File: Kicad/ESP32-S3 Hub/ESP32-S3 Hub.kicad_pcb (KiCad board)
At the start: 6 copper layers, 15 x 30 mm, 57 parts, among them J1 1.27mm 3pin socket, J10 1.27mm 3pin socket, J11 7 pin FPC 0.3mm Panasonic Y3b, J12 1.27mm 3pin socket, J13 TE 3-2363961-0 receptacle, J14 TE 3-2363962-0 Connector, J16 TE 3-2363961-0 receptacle, J17 TE 3-2363962-0 Connector, J2 1.27mm 3pin socket, J21 1.27mm 4 pin socket, J22 1.27mm 4 pin header, J3 7 pin FPC 0.3mm Panasonic Y3b, J4 1.27mm 3pin socket, J5 7 pin FPC 0.3mm Panasonic Y3b, J6 1.27mm 3pin socket, J7 1.27mm 3pin socket, J8 7 pin FPC 0.3mm Panasonic Y3b, J9 1.27mm 3pin socket, SW1 Mitsumi R-667996, SW2 Mitsumi R-667996, U1 ESP32-S3, U2 74HC595, U3 THVD1420DRLR, Y1 ABM11-40.000MHZ-B1U-T3, 10ppm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

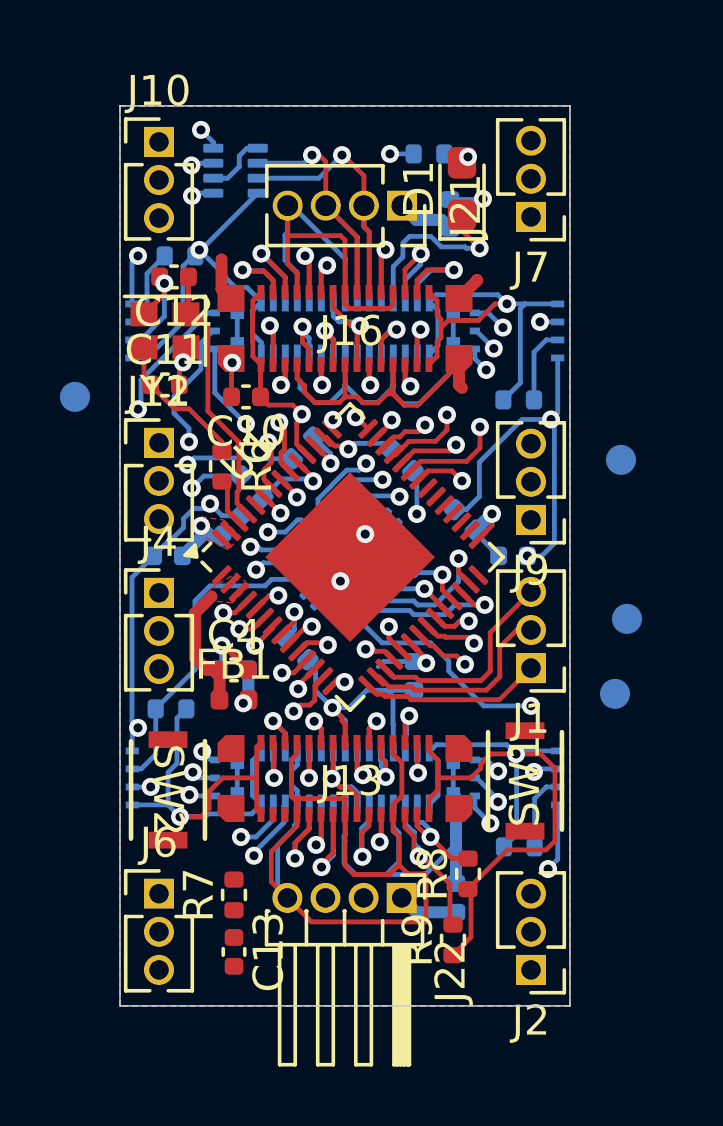
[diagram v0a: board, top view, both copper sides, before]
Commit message: Routed UART, buttons, and flipped analog power cap
I needed a capacitor near the power input at the top, because otherwise the power is flowing directly from the plane through the one via. I'm still not sure that I've fixed a problem, its seems likely that the main power flowing so close to the chips pins is a bad idea.
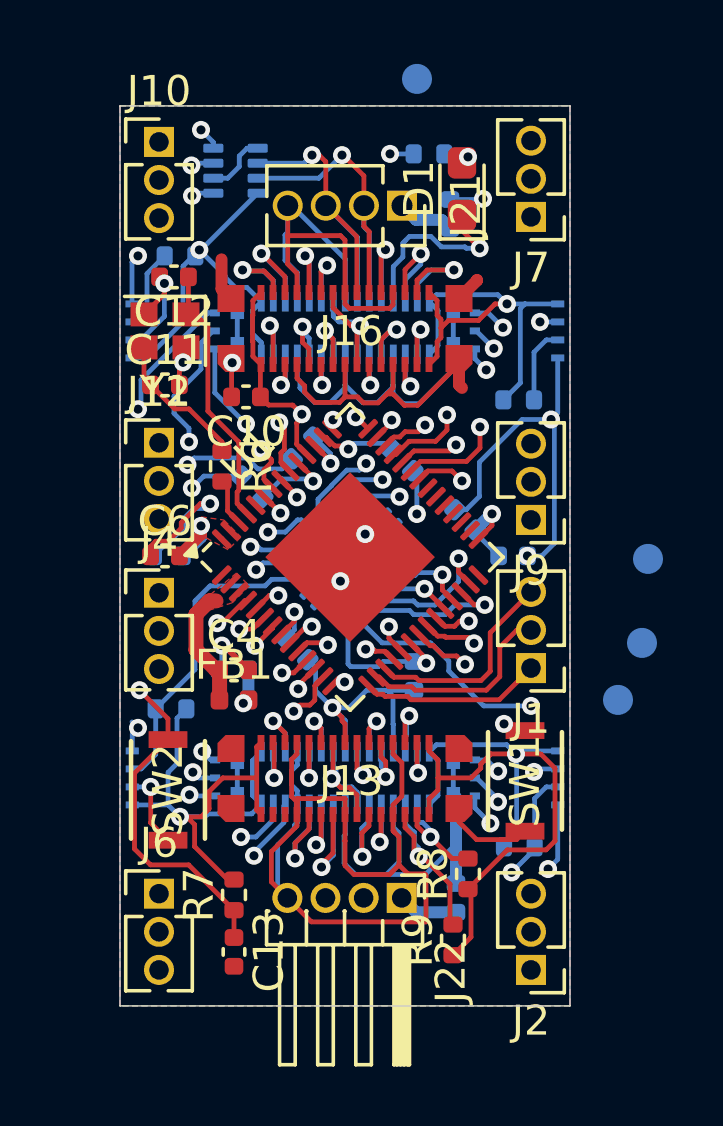
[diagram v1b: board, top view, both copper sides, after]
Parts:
- C6: moved to F.Cu
- moved TP20 15.6 mm to (157.8, 80.9)
- moved TP14 3.42 mm to (165.5, 96.9)
- moved C6 2.42 mm to (149.4, 96.8), turned to 0 degrees
- moved TP12 0.94 mm to (165.3, 99.7)
- moved TP1 0.22 mm to (164.5, 101.6)
- turned SW2 to 90 degrees
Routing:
- net UART0_TX: track 1.58 -> 19.6 mm
- net NRST: track 0.97 -> 16.6 mm, vias 1 -> 2
- net BOOT: track 0.94 -> 16.0 mm, vias 1 -> 2
- net UART0-RTS/CS0: track 2.62 -> 12.6 mm
- net UART0_RX: track 2.54 -> 12.3 mm
- net CS1: track 10.1 -> 17.6 mm, vias 1 -> 2
- net VDD: track 146.4 -> 152.1 mm
- net LED: track 22.6 -> 24.1 mm
- net GND: track 151.3 -> 152.7 mm
- net SDA1: track 47.3 -> 46.4 mm
- net CS5: track 22.6 -> 21.8 mm

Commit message: Routed Free 1 and 2 pins
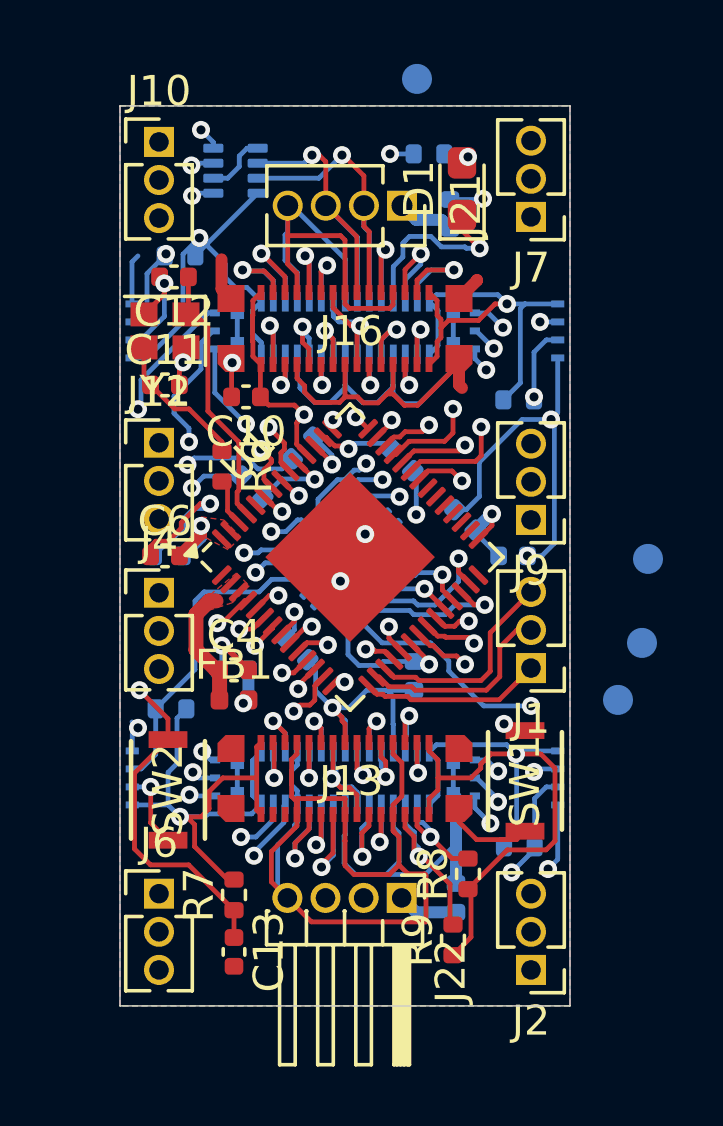
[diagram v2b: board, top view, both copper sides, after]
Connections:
- U1 pad 40: Free1 -> Free2
- U1 pad 41: Free2 -> Free1
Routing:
- net Free2: track 20.9 -> 36.7 mm
- net CS3: track 4.12 -> 16.6 mm, vias 1 -> 2
- net CS4: track 5.23 -> 17.1 mm, vias 1 -> 2
- net Free1: track 16.3 -> 23.0 mm
- net VDD: track 152.1 -> 157.4 mm
- net UART0_TX: track 19.6 -> 15.4 mm
- net SCL1: track 53.6 -> 51.7 mm
- net GND: vias 18 -> 17

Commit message: Swapped header logical numbers
I realized my numbering scheme was off with the actual board layout. So in the schematic I swapped the connectors without rewiring so that the numbers are more logical. CS7, CS8, and Free2 are now for the top mezzanine connector, which is closer to the pins on the chips. It also falls in line with my bottom up numbering scheme.
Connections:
- J13 pad 22: Free2 -> Free1
- J13 pad 26: CS8 -> CS6
- J13 pad 28: CS7 -> CS5
- J13 pad 3: CS7 -> CS5
- J13 pad 5: CS8 -> CS6
- J13 pad 9: Free2 -> Free1
- J14 pad 10: Free2 -> Free1
- J14 pad 21: Free2 -> Free1
- J14 pad 25: CS8 -> CS6
- J14 pad 27: CS7 -> CS5
- J14 pad 4: CS7 -> CS5
- J14 pad 6: CS8 -> CS6
- J16 pad 22: Free1 -> Free2
- J16 pad 26: CS6 -> CS8
- J16 pad 28: CS5 -> CS7
- J16 pad 3: CS5 -> CS7
- J16 pad 5: CS6 -> CS8
- J16 pad 9: Free1 -> Free2
- J17 pad 10: Free1 -> Free2
- J17 pad 21: Free1 -> Free2
- J17 pad 25: CS6 -> CS8
- J17 pad 27: CS5 -> CS7
- J17 pad 4: CS5 -> CS7
- J17 pad 6: CS6 -> CS8
- U1 pad 40: Free2 -> Free1
- U1 pad 41: Free1 -> Free2
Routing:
- net Free2: track 36.7 -> 23.0 mm
- net Free1: track 23.0 -> 36.7 mm
- net CS8: track 15.7 -> 28.0 mm
- net CS6: track 29.5 -> 17.2 mm
- net CS5: track 21.6 -> 12.4 mm
- net CS7: track 13.1 -> 22.3 mm

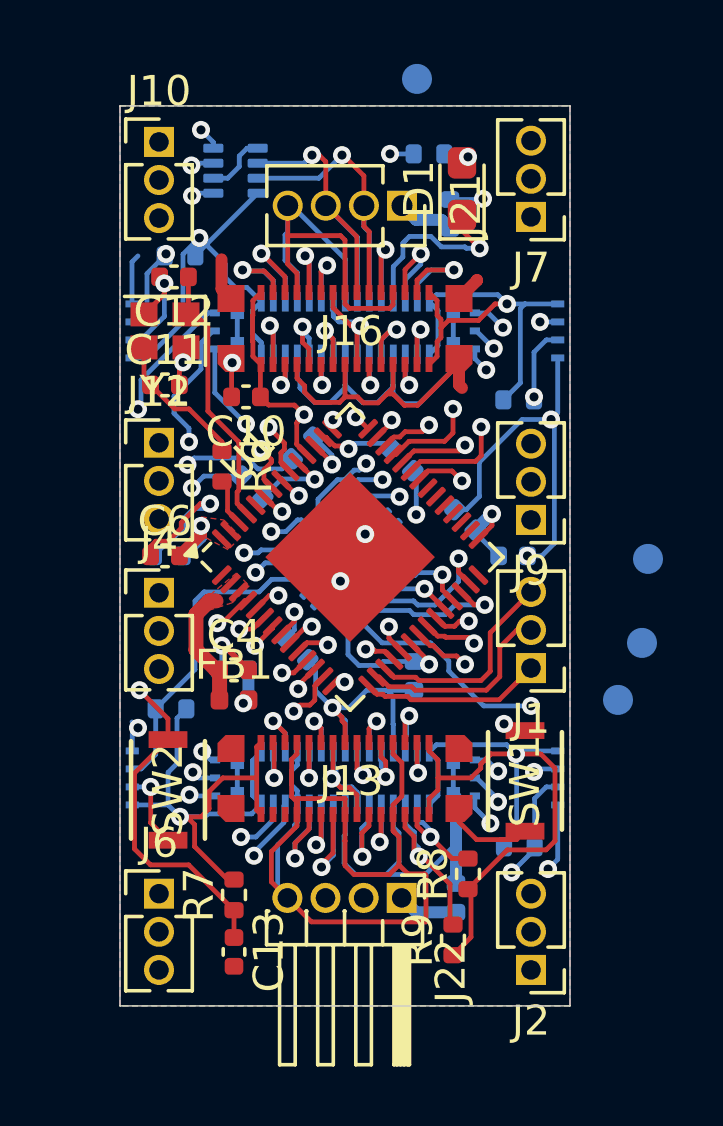
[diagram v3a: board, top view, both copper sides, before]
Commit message: Finished routing PWM motor pins
I did have to sacrifice the continuity of one of my ground planes to make it happen though. I tried to keep it to a minimum
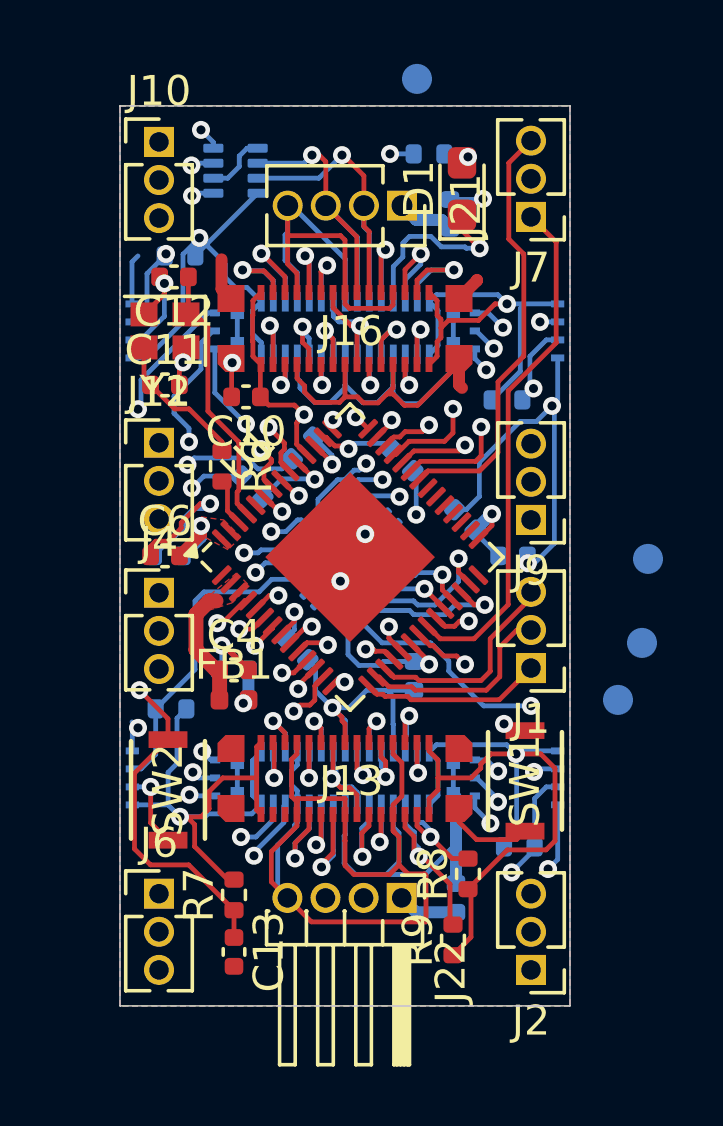
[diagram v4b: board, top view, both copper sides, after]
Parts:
- moved R19 0.39 mm to (160.8, 91.6)
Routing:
- net 4A: track 3.53 -> 21.6 mm
- net 3B: track 1.28 -> 17.6 mm
- net 4B: track 2.34 -> 18.6 mm
- net 3A: track 1.79 -> 17.3 mm, vias 1 -> 0
- net 4C: track 3.07 -> 16.4 mm
- net 3C: track 1.69 -> 14.3 mm, vias 1 -> 0
- net 2C: track 1.94 -> 14.5 mm
- net 2B: track 1.01 -> 11.4 mm
- net 2A: track 1.08 -> 10.3 mm
- net CS3: track 16.6 -> 17.1 mm
- added copper zone on In2.Cu, net VDD
- removed copper zone on In3.Cu, net VDD

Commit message: Finished basic routing
Now I have to fix some things to try and reduce crosstalk, and improve signal integrity. The likelihood of me being able to completely fix it is low, due to limited space. I also have to run the DRC, and fix the silkscreen.
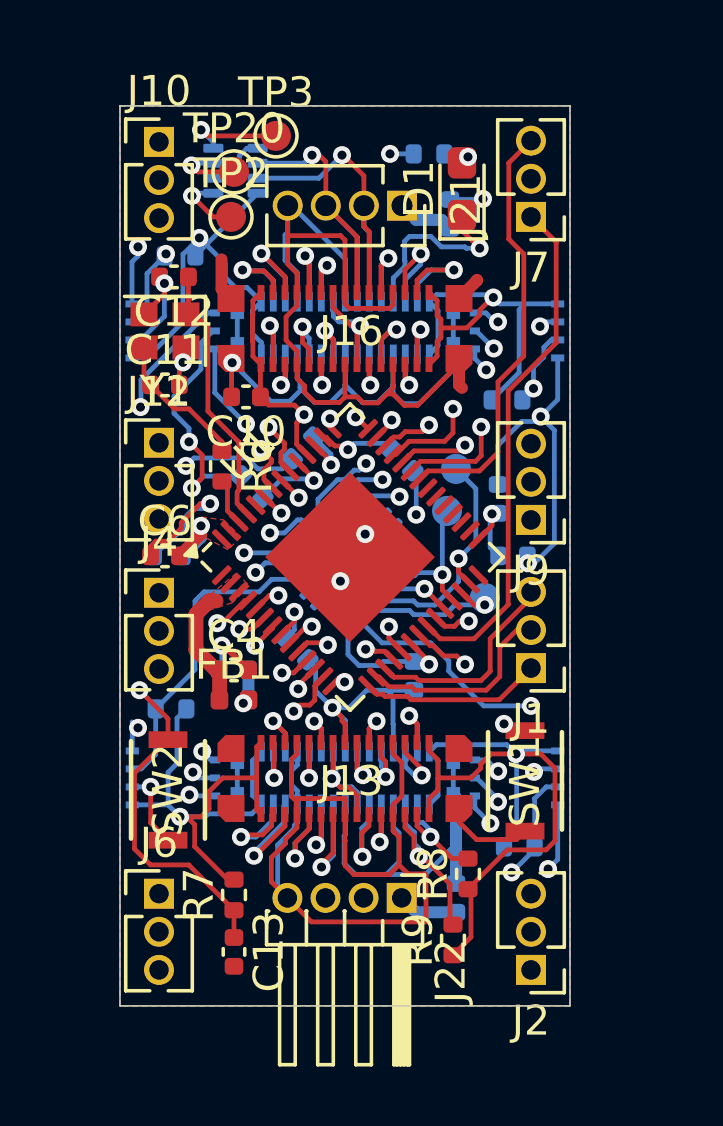
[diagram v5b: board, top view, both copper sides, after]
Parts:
- added TP2: ~, TestPoint:TestPoint_Pad_D1.0mm, F.Cu at (151.6, 85.5)
- added TP3: ~, TestPoint:TestPoint_Pad_D1.0mm, F.Cu at (153.1, 82.8)
- TP20: moved to F.Cu
- moved TP1 9.40 mm to (159.1, 93.9)
- moved TP12 7.85 mm to (158.8, 95.3)
- moved TP20 6.84 mm to (151.7, 84.0), turned to 0 degrees
- moved TP14 5.60 mm to (160.1, 98.2)
- moved C7 1.30 mm to (160.5, 94.9), turned to 90 degrees
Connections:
- TP1 pad 1: ShiftRegCLK -> ShiftEn
- U1 pad 6: 4CSA-B -> 4CSA-A
- U1 pad 7: 4CSA-A -> 4CSA-B
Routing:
- net MISO1: track 38.4 -> 105.8 mm
- net SCK1: track 18.2 -> 65.8 mm
- net MOSI1: track 45.4 -> 93.0 mm
- net VDD: track 157.6 -> 175.5 mm
- net CS6: track 17.2 -> 30.4 mm
- net CS5: track 12.4 -> 25.4 mm
- net CS7: track 22.3 -> 34.6 mm
- net CS8: track 28.0 -> 33.1 mm
- net GND: track 153.0 -> 156.8 mm, vias 17 -> 18
- net ShiftEn: track 5.22 -> 8.72 mm
- net BOOT: track 16.0 -> 12.8 mm
- net UART0_TX: track 15.4 -> 18.1 mm
- net ShiftCLK: track 2.85 -> 5.04 mm
- net 4CSA-A: track 10.8 -> 9.19 mm
- net UART0_RX: track 12.3 -> 13.9 mm
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
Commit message: Cleaned up wires, added IO46 testpad, added license to design files
I also added a ground plane to In3.
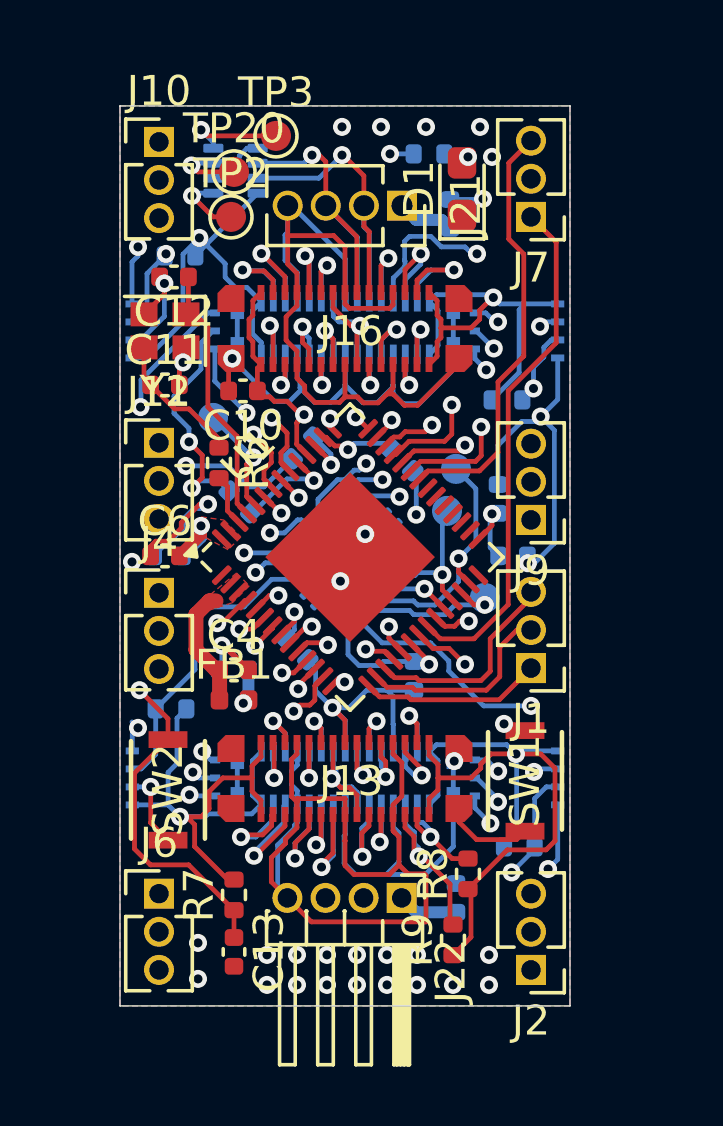
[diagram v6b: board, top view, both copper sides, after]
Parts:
- added TP4: ~, TestPoint:TestPoint_Pad_D1.0mm, B.Cu at (151.0, 92.2)
- moved R5 0.64 mm to (151.9, 95.0)
- moved C10 0.22 mm to (152.0, 91.3)
- moved R6 0.15 mm to (151.2, 93.7)
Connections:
- U1 pad 52: unconnected-(U1-GPIO46-Pad52) -> Net-(U1-GPIO46)
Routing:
- net GND: track 156.8 -> 149.2 mm, vias 18 -> 42
- net Net-(U1-GPIO46): track 0.00 -> 3.70 mm, vias 0 -> 1
- net Free1: track 36.8 -> 34.6 mm
- net CS8: track 33.1 -> 34.5 mm
- net RS485-: track 58.0 -> 57.0 mm
- net Net-(U1-MTDI): track 2.79 -> 3.40 mm
- added copper zone on In3.Cu, net GND

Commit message: Removed problem connections on bottom connector
We don't want several masters fighting over gpio pins or the SPI bus, so I have removed all connections on the bottom side except the multi-master capable busses.
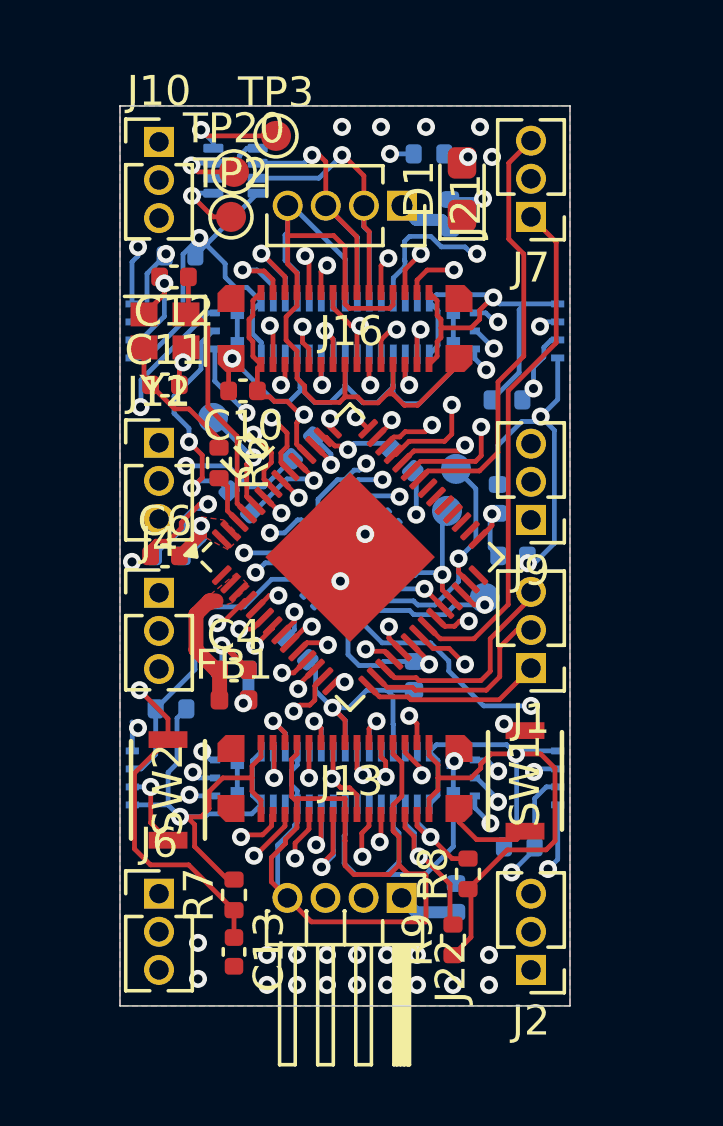
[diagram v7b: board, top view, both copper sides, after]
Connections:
- J14 pad 10: Free1 -> unconnected-(J14-Pin_10-Pad10)
- J14 pad 11: MOSI1 -> unconnected-(J14-Pin_11-Pad11)
- J14 pad 13: SCK1 -> unconnected-(J14-Pin_13-Pad13)
- J14 pad 18: SCK1 -> unconnected-(J14-Pin_18-Pad18)
- J14 pad 20: MOSI1 -> unconnected-(J14-Pin_20-Pad20)
- J14 pad 21: Free1 -> unconnected-(J14-Pin_21-Pad21)
- J14 pad 22: MISO1 -> unconnected-(J14-Pin_22-Pad22)
- J14 pad 25: CS6 -> unconnected-(J14-Pin_25-Pad25)
- J14 pad 27: CS5 -> unconnected-(J14-Pin_27-Pad27)
- J14 pad 4: CS5 -> unconnected-(J14-Pin_4-Pad4)
- J14 pad 6: CS6 -> unconnected-(J14-Pin_6-Pad6)
- J14 pad 9: MISO1 -> unconnected-(J14-Pin_9-Pad9)
- J17 pad 10: Free2 -> unconnected-(J17-Pin_10-Pad10)
- J17 pad 11: MOSI1 -> unconnected-(J17-Pin_11-Pad11)
- J17 pad 13: SCK1 -> unconnected-(J17-Pin_13-Pad13)
- J17 pad 18: SCK1 -> unconnected-(J17-Pin_18-Pad18)
- J17 pad 20: MOSI1 -> unconnected-(J17-Pin_20-Pad20)
- J17 pad 21: Free2 -> unconnected-(J17-Pin_21-Pad21)
- J17 pad 22: MISO1 -> unconnected-(J17-Pin_22-Pad22)
- J17 pad 25: CS8 -> unconnected-(J17-Pin_25-Pad25)
- J17 pad 27: CS7 -> unconnected-(J17-Pin_27-Pad27)
- J17 pad 4: CS7 -> unconnected-(J17-Pin_4-Pad4)
- J17 pad 6: CS8 -> unconnected-(J17-Pin_6-Pad6)
- J17 pad 9: MISO1 -> unconnected-(J17-Pin_9-Pad9)
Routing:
- net SCK1: track 65.5 -> 60.6 mm
- net MISO1: track 106.0 -> 101.3 mm
- net MOSI1: track 93.4 -> 89.2 mm
- net CS6: track 30.4 -> 27.2 mm
- net CS5: track 25.4 -> 22.3 mm
- net CS7: track 34.3 -> 31.2 mm
- net CS8: track 34.5 -> 31.6 mm
- net Free1: track 34.6 -> 31.7 mm
- net Free2: track 21.7 -> 19.3 mm
